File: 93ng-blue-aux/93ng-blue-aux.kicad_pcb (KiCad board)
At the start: 2 copper layers, 3 parts, among them U1 ESP32-WROOM-32D, U2 MCP1703A-3302_SOT223, U3 MC33897

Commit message: More work on schematic, focus on debugging utility, and started layout of PCB. Made footprint for BM62.
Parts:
- added C1: 0.1uF, Capacitor_SMD:C_0805_2012Metric_Pad1.15x1.40mm_HandSolder, F.Cu at (120.9, 141.4)
- added C2: 4.7uF, Capacitor_SMD:C_0805_2012Metric_Pad1.15x1.40mm_HandSolder, F.Cu at (120.8, 135.5)
- added C3: 0.1uF, Capacitor_SMD:C_0805_2012Metric_Pad1.15x1.40mm_HandSolder, F.Cu at (189.2, 94.0)
- added C4: 47pF, Capacitor_SMD:C_0805_2012Metric_Pad1.15x1.40mm_HandSolder, F.Cu at (125.5, 135.5)
- added D1: D, Diode_SMD:D_0805_2012Metric_Pad1.15x1.40mm_HandSolder, F.Cu at (117.2, 110.5)
- added D2: LED, LED_SMD:LED_0805_2012Metric_Pad1.15x1.40mm_HandSolder, F.Cu at (115.6, 94.0)
- added D3: MMBZ15VDLT1, Package_TO_SOT_SMD:SOT-23, F.Cu at (110.5, 107.3)
- added D4: LED, LED_SMD:LED_0805_2012Metric_Pad1.15x1.40mm_HandSolder, F.Cu at (115.6, 89.5)
- added J1: 12V INPUT, Connector_PinHeader_2.54mm:PinHeader_1x02_P2.54mm_Vertical, F.Cu at (95.9, 90.8)
- added J2: ESP32 UART, Connector_PinHeader_2.54mm:PinHeader_1x03_P2.54mm_Vertical, F.Cu at (155.6, 59.1)
- added J3: ESP32 JTAG, Connector_PinHeader_2.54mm:PinHeader_1x04_P2.54mm_Vertical, F.Cu at (149.2, 59.1)
- added J4: AUX OUT, Connector_Audio:Jack_3.5mm_CUI_SJ-3523-SMT_Horizontal, F.Cu at (102.9, 69.8)
- added J5: MIC IN, Connector_Audio:Jack_3.5mm_CUI_SJ-3523-SMT_Horizontal, F.Cu at (102.9, 81.3)
- added J6: BM62 UART, Connector_PinHeader_2.54mm:PinHeader_1x03_P2.54mm_Vertical, F.Cu at (119.4, 88.9)
- added L1: 47uH, Inductor_SMD:L_0805_2012Metric_Pad1.15x1.40mm_HandSolder, F.Cu at (120.8, 138.4)
- added R1: 1k, Resistor_SMD:R_0805_2012Metric_Pad1.15x1.40mm_HandSolder, F.Cu at (181.0, 89.5)
- added R10: 1k, Resistor_SMD:R_0805_2012Metric_Pad1.15x1.40mm_HandSolder, F.Cu at (125.5, 138.4)
- added R2: 100, Resistor_SMD:R_0805_2012Metric_Pad1.15x1.40mm_HandSolder, F.Cu at (116.1, 142.1)
- added R3: 100, Resistor_SMD:R_0805_2012Metric_Pad1.15x1.40mm_HandSolder, F.Cu at (116.1, 145.1)
- added R4: 100, Resistor_SMD:R_0805_2012Metric_Pad1.15x1.40mm_HandSolder, F.Cu at (130.3, 132.4)
- added R5: 100, Resistor_SMD:R_0805_2012Metric_Pad1.15x1.40mm_HandSolder, F.Cu at (135.9, 91.4)
- added R6: 10k, Resistor_SMD:R_0805_2012Metric_Pad1.15x1.40mm_HandSolder, F.Cu at (116.1, 148.0)
- added R7: 2.7k, Resistor_SMD:R_0805_2012Metric_Pad1.15x1.40mm_HandSolder, F.Cu at (190.3, 100.3)
- added R8: 1k, Resistor_SMD:R_0805_2012Metric_Pad1.15x1.40mm_HandSolder, F.Cu at (120.9, 144.3)
- added R9: 6.49k, Resistor_SMD:R_0805_2012Metric_Pad1.15x1.40mm_HandSolder, F.Cu at (121.9, 110.5)
- added SW1: SYS CONFIG, Button_Switch_SMD:SW_DIP_SPSTx04_Slide_Omron_A6S-410x_W8.9mm_P2.54mm, F.Cu at (165.7, 62.9)
- added TP1: TX_COND, TestPoint:TestPoint_Pad_D2.0mm, F.Cu at (117.5, 69.2)
- added TP2: FWD, TestPoint:TestPoint_Pad_D2.0mm, F.Cu at (141.0, 84.5)
- added TP3: REV, TestPoint:TestPoint_Pad_D2.0mm, F.Cu at (141.0, 76.2)
- added TP4: VOL+, TestPoint:TestPoint_Pad_D2.0mm, F.Cu at (144.8, 72.4)
- added TP5: PLAY/PAUSE, TestPoint:TestPoint_Pad_D2.0mm, F.Cu at (144.8, 80.0)
- added TP6: VOL-, TestPoint:TestPoint_Pad_D2.0mm, F.Cu at (148.6, 76.2)
- added U4: BM62SPKS1MC2-0001AA, custom_footprints:BM62SPKS1MC2-0001AA, F.Cu at (121.9, 86.4)
- U2: value MCP1703A-3302_SOT223 -> BA33DD0T; footprint Package_TO_SOT_SMD:SOT-223-3_TabPin2 -> Package_TO_SOT_THT:TO-220-3_Vertical
- U3: footprint custom_footprints:MC33897 -> Package_SO:SOIC-14_3.9x8.7mm_P1.27mm
- moved U2 60.7 mm to (103.5, 91.4), turned to 270 degrees
- moved U3 44.9 mm to (121.3, 103.5), turned to 270 degrees
- moved U1 44.5 mm to (161.9, 82.5), turned to 180 degrees
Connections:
- U1 pad 1: Net-(U1-Pad1) -> GND
- U1 pad 11: Net-(U1-Pad11) -> BM62_MCU_WAKE
- U1 pad 12: Net-(U1-Pad12) -> BM62_BT_WAKE
- U1 pad 15: Net-(U1-Pad1) -> GND
- U1 pad 2: Net-(U1-Pad2) -> 3.3V
- U1 pad 25: Net-(U1-Pad25) -> ESP32_BOOTOPT
- U1 pad 27: Net-(U1-Pad27) -> MC33_RX
- U1 pad 28: Net-(U1-Pad28) -> MC33_TX
- U1 pad 30: Net-(U1-Pad30) -> MC33_MODE0
- U1 pad 31: Net-(U1-Pad31) -> MC33_MODE1
- U1 pad 38: Net-(U1-Pad1) -> GND
- U1 pad 39: Net-(U1-Pad1) -> GND
- U1 pad 8: Net-(U1-Pad8) -> BM62_RX
- U1 pad 9: Net-(U1-Pad9) -> BM62_TX
- U2 pad 2: Net-(U2-Pad2) -> GND
- U2 pad 3: Net-(U2-Pad3) -> 3.3V
- U3 pad 1: Net-(U3-Pad1) -> GND
- U3 pad 14: Net-(U3-Pad14) -> GND
- U3 pad 2: Net-(U3-Pad2) -> MC33_TX
- U3 pad 3: Net-(U3-Pad3) -> MC33_MODE0
- U3 pad 4: Net-(U3-Pad4) -> MC33_MODE1
- U3 pad 5: Net-(U3-Pad5) -> MC33_RX
- U3 pad 7: Net-(U3-Pad7) -> GND
- U3 pad 8: Net-(U3-Pad8) -> GND
- U3 pad 9: Net-(U3-Pad9) -> 3.3V

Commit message: Added picture of schematic. Added some screw terminals.
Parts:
- added J7: I-BUS, TerminalBlock_Phoenix:TerminalBlock_Phoenix_MKDS-3-2-5.08_1x02_P5.08mm_Horizontal, F.Cu at (164.0, 121.9)
- J1: footprint Connector_PinHeader_2.54mm:PinHeader_1x02_P2.54mm_Vertical -> TerminalBlock_Phoenix:TerminalBlock_Phoenix_MKDS-3-2-5.08_1x02_P5.08mm_Horizontal
- moved J1 7.24 mm to (100.3, 96.5), turned to 90 degrees
- moved U2 6.35 mm to (109.9, 91.4)
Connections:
- J1 pad 1: Net-(J1-Pad1) -> GND
- J1 pad 2: GND -> Net-(J1-Pad2)
- U2 pad 1: Net-(J1-Pad1) -> Net-(J1-Pad2)

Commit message: Completed roughest PCB layout ever
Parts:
- moved C3 115.4 mm to (74.0, 88.0), turned to 270 degrees
- moved J7 110.8 mm to (57.0, 93.0), turned to 90 degrees
- moved R3 92.2 mm to (130.5, 54.0)
- moved R2 85.8 mm to (130.5, 57.5)
- moved R7 82.6 mm to (110.5, 79.0), turned to 270 degrees
- moved R6 77.5 mm to (74.0, 83.0), turned to 90 degrees
- moved C2 71.0 mm to (82.0, 76.0)
- moved R4 68.4 mm to (130.5, 64.0)
- moved SW1 67.3 mm to (102.5, 86.0), turned to 180 degrees
- moved TP2 66.9 mm to (75.0, 73.5)
- moved TP3 66.9 mm to (75.0, 65.2)
- moved TP4 66.9 mm to (78.8, 61.4)
- moved TP5 66.9 mm to (78.8, 69.0)
- moved TP6 66.9 mm to (82.6, 65.2)
- moved R8 64.2 mm to (94.0, 86.0)
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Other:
- board outline added: 88 x 50 mm

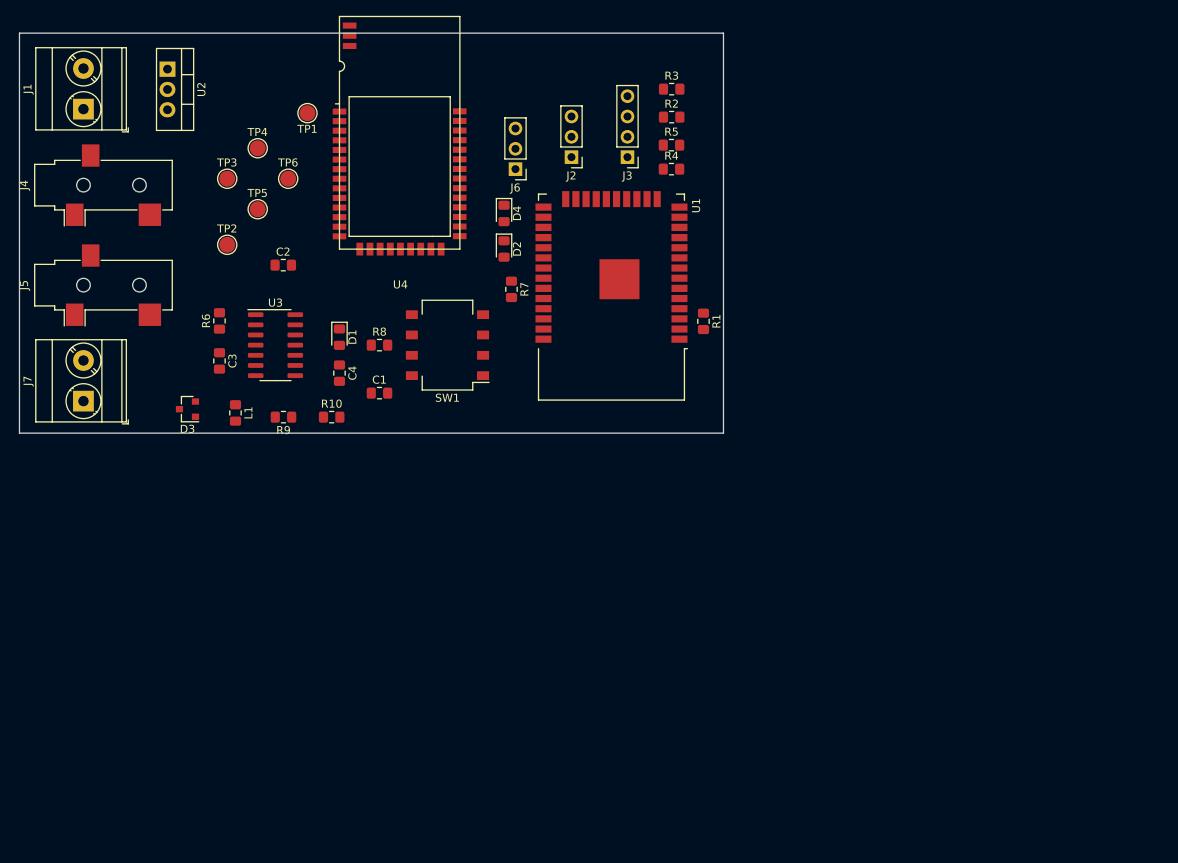
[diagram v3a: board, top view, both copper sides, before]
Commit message: Working on 100mmx100mm board design. Adjusted input power filter cap size. Re-designed bluetooth antenna keepout comment, and added courtyard to module.
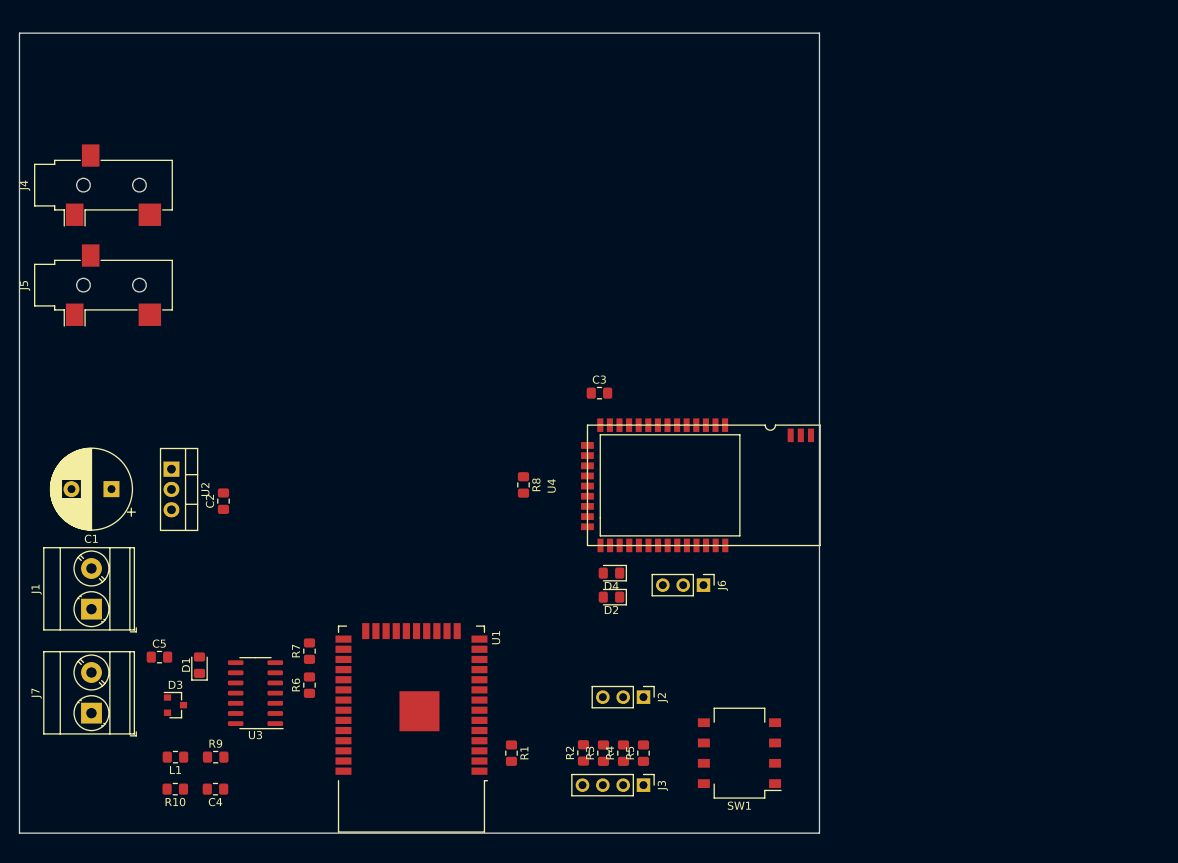
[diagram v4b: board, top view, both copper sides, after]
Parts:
- removed TP1: TX_COND, TestPoint:TestPoint_Pad_D2.0mm
- removed TP2: FWD, TestPoint:TestPoint_Pad_D2.0mm
- removed TP3: REV, TestPoint:TestPoint_Pad_D2.0mm
- removed TP4: VOL+, TestPoint:TestPoint_Pad_D2.0mm
- removed TP5: PLAY/PAUSE, TestPoint:TestPoint_Pad_D2.0mm
- removed TP6: VOL-, TestPoint:TestPoint_Pad_D2.0mm
- added C1: 10uF, Capacitor_THT:CP_Radial_D10.0mm_P5.00mm, F.Cu at (60.5, 104.0)
- moved R3 83.4 mm to (122.0, 137.0), turned to 90 degrees
- moved R2 80.2 mm to (119.5, 137.0), turned to 90 degrees
- moved J3 78.5 mm to (127.0, 141.0), turned to 270 degrees
- moved R5 76.1 mm to (127.0, 137.0), turned to 90 degrees
- moved R4 73.2 mm to (124.5, 137.0), turned to 90 degrees
- moved J2 68.1 mm to (127.0, 130.0), turned to 270 degrees
- moved SW1 62.7 mm to (139.0, 137.0)
- moved J1 62.5 mm to (58.0, 119.0)
- moved U1 59.5 mm to (98.0, 131.0)
- moved R1 59.1 mm to (110.5, 137.0)
- moved J6 57.1 mm to (134.5, 116.0), turned to 270 degrees
- moved C4 53.5 mm to (73.5, 141.5), turned to 180 degrees
- moved R7 51.8 mm to (85.2, 124.2), turned to 90 degrees
- moved R10 50.4 mm to (68.5, 141.5), turned to 180 degrees
- moved U2 50.0 mm to (68.0, 101.5)
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- renumbered C1 to C2, C2 to C3, C3 to C4, C4 to C5
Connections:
- U1 pad 10: Net-(U1-Pad10) -> (no net)
- U1 pad 17: Net-(U1-Pad17) -> (no net)
- U1 pad 18: Net-(U1-Pad18) -> (no net)
- U1 pad 19: Net-(U1-Pad19) -> (no net)
- U1 pad 20: Net-(U1-Pad20) -> (no net)
- U1 pad 21: Net-(U1-Pad21) -> (no net)
- U1 pad 22: Net-(U1-Pad22) -> (no net)
- U1 pad 24: Net-(U1-Pad24) -> (no net)
- U1 pad 26: Net-(U1-Pad26) -> (no net)
- U1 pad 29: Net-(U1-Pad29) -> (no net)
- U1 pad 32: Net-(U1-Pad32) -> (no net)
- U1 pad 33: Net-(U1-Pad33) -> (no net)
- U1 pad 36: Net-(U1-Pad36) -> (no net)
- U1 pad 37: Net-(U1-Pad37) -> (no net)
- U1 pad 4: Net-(U1-Pad4) -> (no net)
- U1 pad 5: Net-(U1-Pad5) -> (no net)
- U1 pad 6: Net-(U1-Pad6) -> (no net)
- U1 pad 7: Net-(U1-Pad7) -> (no net)
- U3 pad 13: Net-(U3-Pad13) -> (no net)
- U3 pad 6: Net-(U3-Pad6) -> (no net)
- U4 pad 10: Net-(U4-Pad10) -> (no net)
- U4 pad 14: Net-(U4-Pad14) -> (no net)
- U4 pad 15: Net-(U4-Pad15) -> (no net)
- U4 pad 17: Net-(U4-Pad17) -> (no net)
- U4 pad 18: Net-(TP2-Pad1) -> (no net)
- U4 pad 19: Net-(U4-Pad19) -> (no net)
- U4 pad 20: Net-(U4-Pad20) -> (no net)
- U4 pad 22: Net-(U4-Pad22) -> (no net)
- U4 pad 25: Net-(U4-Pad25) -> (no net)
- U4 pad 3: Net-(U4-Pad3) -> (no net)
- U4 pad 30: Net-(TP5-Pad1) -> (no net)
- U4 pad 31: Net-(TP3-Pad1) -> (no net)
- U4 pad 34: Net-(TP6-Pad1) -> (no net)
- U4 pad 35: Net-(TP4-Pad1) -> (no net)
- U4 pad 36: Net-(U4-Pad36) -> (no net)
- U4 pad 38: Net-(U4-Pad38) -> (no net)
- U4 pad 39: Net-(U4-Pad39) -> (no net)
- U4 pad 40: Net-(U4-Pad40) -> (no net)
- U4 pad 5: Net-(U4-Pad5) -> (no net)
- U4 pad 6: Net-(U4-Pad6) -> (no net)
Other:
- board size 88 x 50 mm -> 100 x 100 mm

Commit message: PCB Layout progress.
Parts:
- moved C3 32.0 mm to (95.8, 111.0), turned to 90 degrees
- moved J4 31.8 mm to (77.5, 92.2), turned to 0 degrees
- moved SW1 26.9 mm to (128.9, 112.0)
- moved U4 25.5 mm to (100.5, 112.5), turned to 0 degrees
- moved R2 22.9 mm to (105.2, 119.0), turned to 180 degrees
- moved R3 19.8 mm to (113.8, 119.0), turned to 180 degrees
- moved C1 17.7 mm to (73.5, 116.0)
- moved C2 17.0 mm to (87.0, 117.0)
- moved U2 17.0 mm to (80.0, 113.5)
- moved R4 16.0 mm to (120.5, 121.5), turned to 180 degrees
- moved J5 14.9 mm to (65.5, 92.2), turned to 0 degrees
- moved R5 14.5 mm to (120.5, 124.0), turned to 180 degrees
- moved J3 14.1 mm to (125.5, 127.0), turned to 90 degrees
- moved R8 13.4 mm to (105.2, 115.0), turned to 0 degrees
- moved D2 11.4 mm to (120.0, 106.5), turned to 0 degrees
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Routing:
- net GND: track 0.00 -> 141.2 mm, vias 0 -> 2
- net 3.3V: track 0.00 -> 102.2 mm, vias 0 -> 2
- net Net-(C1-Pad1): track 0.00 -> 23.9 mm
- net SW_CAN: track 0.00 -> 23.9 mm
- net MC33_TX: track 0.00 -> 21.8 mm
- net MC33_RX: track 0.00 -> 19.8 mm
- net MC33_MODE0: track 0.00 -> 19.6 mm, vias 0 -> 2
- net MC33_MODE1: track 0.00 -> 18.1 mm, vias 0 -> 2
- net Net-(C4-Pad2): track 0.00 -> 16.2 mm
- net Net-(R9-Pad2): track 0.00 -> 9.10 mm
- net Net-(C4-Pad1): track 0.00 -> 6.85 mm
- net Net-(R1-Pad1): track 0.00 -> 4.31 mm
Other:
- board size 100 x 100 mm -> 87.5 x 64 mm
- board text added: "12V TO 3.3V REGULATOR"
- board text added: "AUDIO INTERFACE"
- board text added: "PROGRAM INTERFACE"
- board text added: "SW-CAN INTERFACE"

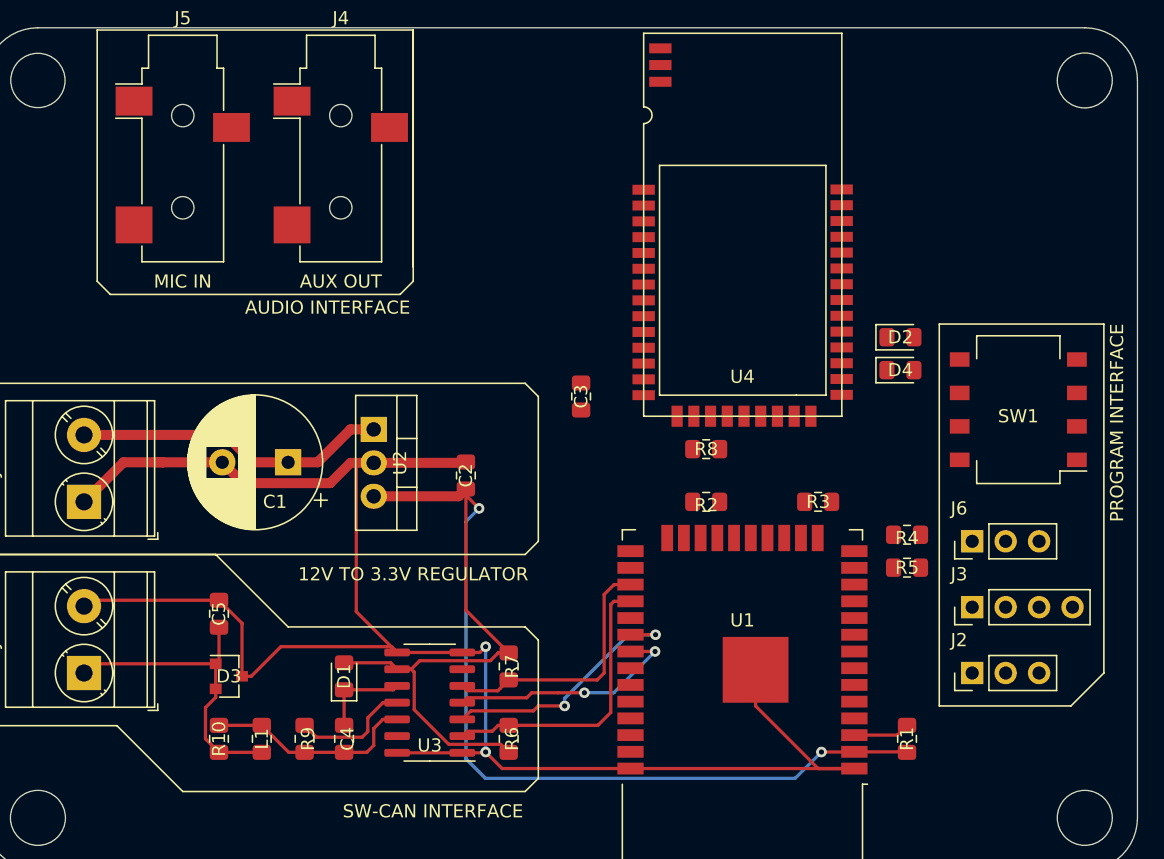
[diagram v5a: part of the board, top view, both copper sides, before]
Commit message: Finished trace layout.
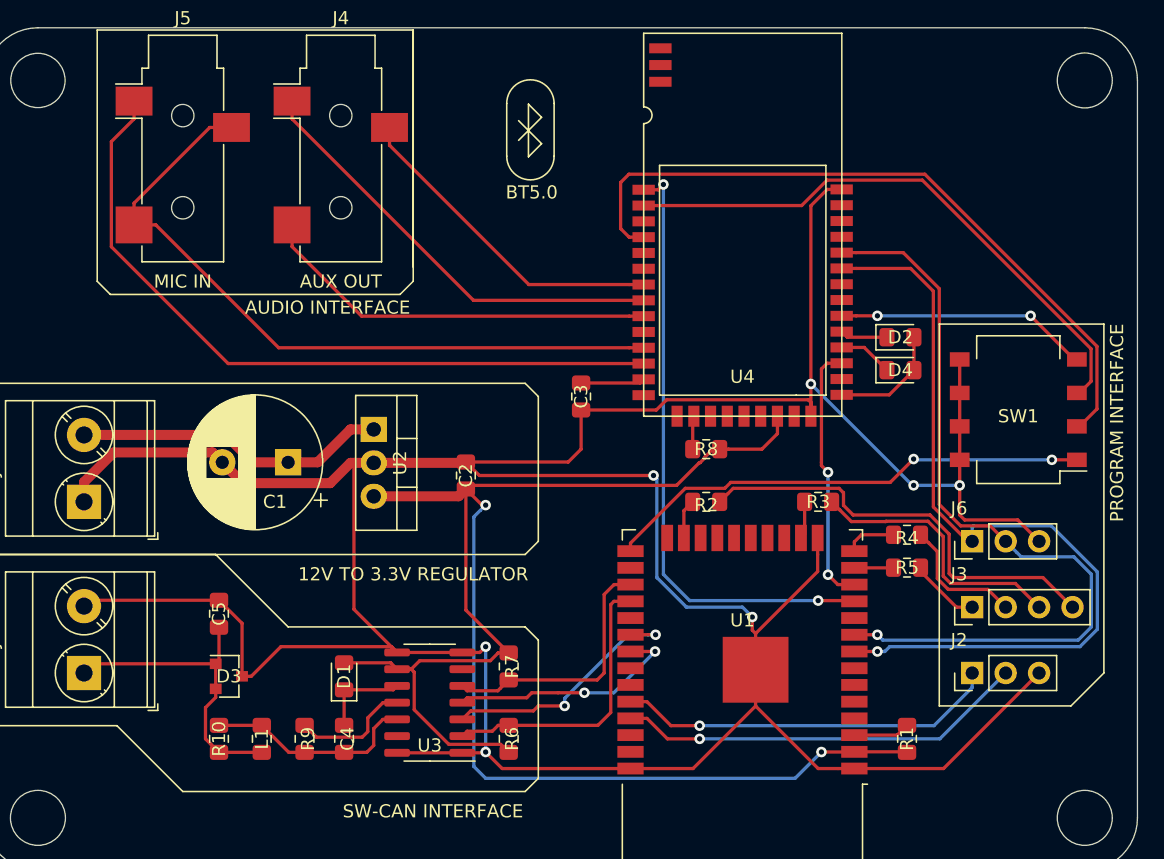
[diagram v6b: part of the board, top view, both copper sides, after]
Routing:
- net GND: track 141.2 -> 281.3 mm, vias 2 -> 7
- net BM62_RX: track 0.00 -> 63.7 mm, vias 0 -> 1
- net BM62_TX: track 0.00 -> 61.3 mm, vias 0 -> 1
- net Net-(J5-PadS): track 0.00 -> 55.9 mm
- net BM62_P2_0: track 0.00 -> 54.2 mm
- net Net-(J5-PadR): track 0.00 -> 54.0 mm
- net BM62_MCU_WAKE: track 0.00 -> 46.6 mm, vias 0 -> 2
- net BM62_EAN: track 0.00 -> 44.0 mm
- net ESP32_BOOTOPT: track 0.00 -> 37.2 mm, vias 0 -> 2
- net Net-(J4-PadS): track 0.00 -> 33.8 mm
- net Net-(J3-Pad4): track 0.00 -> 33.3 mm
- net Net-(J2-Pad2): track 0.00 -> 31.2 mm, vias 0 -> 1
- net Net-(J4-PadT): track 0.00 -> 30.5 mm
- net Net-(J2-Pad1): track 0.00 -> 29.0 mm, vias 0 -> 1
- net 3.3V: track 102.2 -> 129.0 mm
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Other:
- board text added: "BT5.0"
